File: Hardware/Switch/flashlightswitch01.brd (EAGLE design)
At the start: 38.1 x 50.8 mm, 19 parts

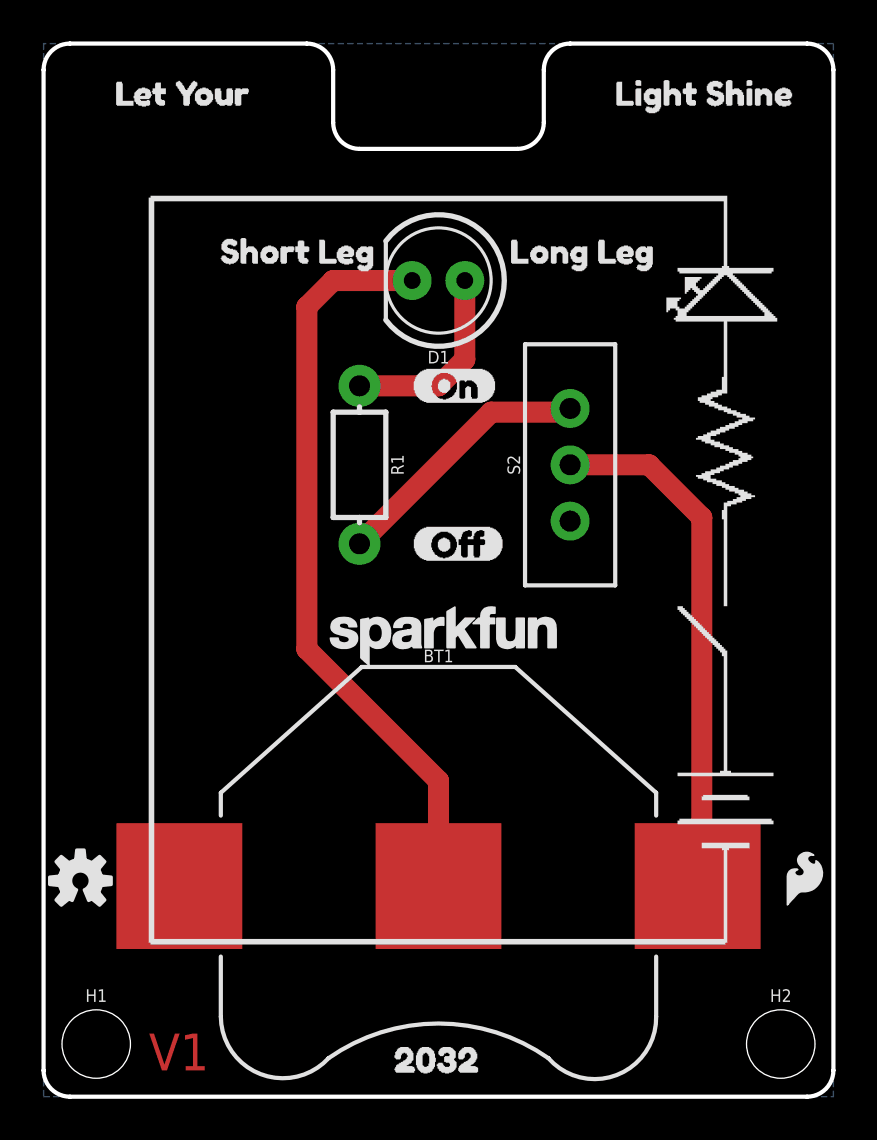
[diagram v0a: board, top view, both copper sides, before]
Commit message: Post Proto Review
Added Buzzard labels, changed to different coin cell battery holder, moved schematic to back of board and other changes.
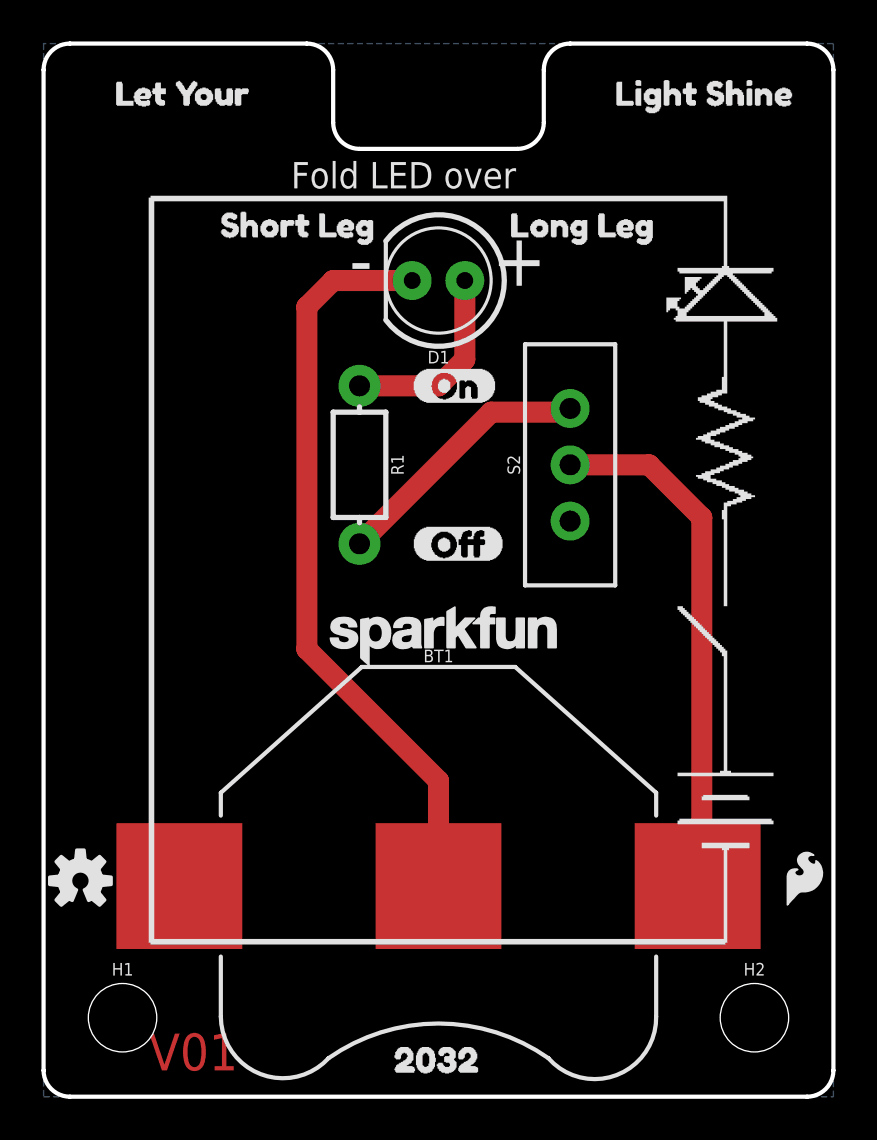
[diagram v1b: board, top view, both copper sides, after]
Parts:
- R1: value (none) -> 330
- moved H2 1.80 mm to (34.3, 3.81)
- moved H1 1.80 mm to (3.81, 3.81)
- moved U$7 1.27 mm to (7.62, 41.9)
- moved U$8 1.27 mm to (21.6, 41.9)
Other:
- board text added: "+"
- board text added: "-"
- board text added: "Battery"
- board text added: "Fold LED over"
- board text added: "LED"
- board text added: "Resistor"
- board text added: "Switch"
- board text added: "V01"
- board text removed: "Battery - This powers your circuit"
- board text removed: "LED (Light Emitting Diode) - This is your light."
- board text removed: "Resistor - This limits the current your LED recieves"
- board text removed: "Switch - This completes your circuit"
- board text removed: "V1"
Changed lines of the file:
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@@
 <layers>
 <layer number="1" name="Top" color="4" fill="1" visible="yes" active="yes"/>
-<layer number="16" name="Bottom" color="1" fill="1" visible="yes" active="yes"/>
+<layer number="16" name="Bottom" color="1" fill="1" visible="no" active="yes"/>
 <layer number="17" name="Pads" color="2" fill="1" visible="yes" active="yes"/>
 <layer number="18" name="Vias" color="2" fill="1" visible="yes" active="yes"/>
@@
 <layer number="20" name="Dimension" color="15" fill="1" visible="yes" active="yes"/>
 <layer number="21" name="tPlace" color="16" fill="1" visible="yes" active="yes"/>
-<layer number="22" name="bPlace" color="14" fill="1" visible="yes" active="yes"/>
+<layer number="22" name="bPlace" color="14" fill="1" visible="no" active="yes"/>
 <layer number="23" name="tOrigins" color="15" fill="1" visible="yes" active="yes"/>
 <layer number="24" name="bOrigins" color="15" fill="1" visible="yes" active="yes"/>
@@
 <layer number="47" name="Measures" color="7" fill="1" visible="no" active="yes"/>
 <layer number="48" name="Document" color="7" fill="1" visible="no" active="yes"/>
-<layer number="49" name="Reference" color="7" fill="1" visible="yes" active="yes"/>
+<layer number="49" name="Reference" color="7" fill="1" visible="no" active="yes"/>
 <layer number="50" name="dxf" color="7" fill="1" visible="no" active="yes"/>
 <layer number="51" name="tDocu" color="6" fill="1" visible="yes" active="yes"/>
@@
 <board>
 <plain>
-<text x="36.83" y="40.64" size="1.27" layer="22" font="vector" ratio="15" rot="MR0" align="top-left">LED (Light
-Emitting Diode) -
-This is your
-light.</text>
-<text x="1.27" y="34.29" size="1.27" layer="22" font="vector" ratio="15" rot="MR0" align="top-right">Resistor -
-This limits
-the current
-your LED
-recieves</text>
-<text x="36.83" y="25.4" size="1.27" layer="22" font="vector" ratio="15" rot="MR0" align="top-left">Switch - This
-completes
-your circuit</text>
-<text x="27.94" y="15.24" size="1.27" layer="22" font="vector" ratio="15" rot="MR0" align="top-left">Battery - This
-powers your circuit</text>
+<text x="20.32" y="36.83" size="1.27" layer="22" font="vector" ratio="15" rot="MR0" align="top-left">LED </text>
+<text x="12.7" y="34.29" size="1.27" layer="22" font="vector" ratio="15" rot="MR90" align="top-right">Resistor</text>
+<text x="27.94" y="33.02" size="1.27" layer="22" font="vector" ratio="15" rot="MR270" align="top-left">Switch</text>
+<text x="22.86" y="12.7" size="1.27" layer="22" font="vector" ratio="15" rot="MR0" align="top-left">Battery</text>
 <wire x1="15.24" y1="45.72" x2="22.86" y2="45.72" width="0.2032" layer="20"/>
 <wire x1="38.1" y1="49.53" x2="38.1" y2="1.27" width="0.2032" layer="20"/>
@@
 <wire x1="13.97" y1="46.99" x2="15.24" y2="45.72" width="0.2032" layer="20" curve="90"/>
 <wire x1="0" y1="49.53" x2="1.27" y2="50.8" width="0.2032" layer="20" curve="-90"/>
-<text x="31.75" y="43.18" size="1.778" layer="22" rot="MR0">sparkfun.com/flashlight</text>
+<text x="34.29" y="43.18" size="1.778" layer="22" font="vector" rot="MR0">sparkfun.com/flashlight</text>
 <text x="36.83" y="48.26" size="1.778" layer="22" rot="MR0">Flashlight</text>
-<text x="5.08" y="1.27" size="1.778" layer="1">V1</text>
+<text x="5.08" y="1.27" size="1.778" layer="1" font="vector" ratio="15">V01</text>
+<text x="15.875" y="39.116" size="2.54" layer="21" font="vector" rot="MR0">-</text>
+<text x="24.257" y="39.116" size="2.54" layer="21" font="vector" rot="MR0">+</text>
+<text x="11.938" y="43.815" size="1.27" layer="21" font="vector" ratio="15">Fold LED over</text>
 </plain>
 <attributes>
@@
 <element name="FRAME1" library="SparkFun-Aesthetics" package="CREATIVE_COMMONS" value="FRAME-LETTER" x="20.32" y="-8.89"/>
 <element name="LOGO1" library="SparkFun-Aesthetics" package="OSHW-LOGO-S" value="OSHW-LOGOS" x="1.778" y="10.414"/>
-<element name="R1" library="SparkFun-Resistors" package="AXIAL-0.3-KIT" value=" " x="15.24" y="30.48" rot="R270">
+<element name="R1" library="SparkFun-Resistors" package="AXIAL-0.3-KIT" value="330" x="15.24" y="30.48" rot="R270">
 <attribute name="PROD_ID" value=" " x="15.24" y="30.48" size="1.778" layer="27" rot="R270" display="off"/>
 </element>
 <element name="LOGO2" library="SparkFun-Aesthetics" package="SFE_LOGO_FLAME_.1" value="SFE_LOGO_FLAME.1_INCH" x="35.56" y="8.89"/>
-<element name="H1" library="SparkFun-Hardware" package="STAND-OFF" value="STAND-OFF" x="2.54" y="2.54"/>
-<element name="H2" library="SparkFun-Hardware" package="STAND-OFF" value="STAND-OFF" x="35.56" y="2.54"/>
+<element name="H1" library="SparkFun-Hardware" package="STAND-OFF" value="STAND-OFF" x="3.81" y="3.81"/>
+<element name="H2" library="SparkFun-Hardware" package="STAND-OFF" value="STAND-OFF" x="34.29" y="3.81"/>
 <element name="U$1" library="flashlight2#png" package="FLASHLIGHT2#PNG" value="" x="20.32" y="25.4"/>
 <element name="S2" library="SparkFun-Switches" package="SWITCH_SPDT_PTH_11.6X4.0MM_KIT" value="" x="25.4" y="30.48">
@@
 <element name="U$5" library="buzzard_labels" package="LIGHT_SHINE0" value="" x="26.67" y="48.26"/>
 <element name="U$6" library="buzzard_labels" package="LET_YOUR0" value="" x="2.54" y="48.26"/>
-<element name="U$7" library="buzzard_labels" package="SHORT_LEG0" value="" x="7.62" y="40.64"/>
-<element name="U$8" library="buzzard_labels" package="LONG_LEG0" value="" x="21.59" y="40.64"/>
+<element name="U$7" library="buzzard_labels" package="SHORT_LEG0" value="" x="7.62" y="41.91"/>
+<element name="U$8" library="buzzard_labels" package="LONG_LEG0" value="" x="21.59" y="41.91"/>
 <element name="LOGO3" library="SparkFun-Aesthetics" package="SFE_LOGO_NAME_FLAME_.2" value="SFE_LOGO_NAME_FLAME.2_INCH" x="31.75" y="0" rot="MR0"/>
 </elements>
@@
 </board>
 </drawing>
-<compatibility>
-<note version="6.3" minversion="6.2.2" severity="warning">
-Since Version 6.2.2 text objects can contain more than one line,
-which will not be processed correctly with this version.
-</note>
-</compatibility>
 </eagle>
